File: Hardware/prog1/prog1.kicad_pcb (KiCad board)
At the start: 2 copper layers, 16 x 21 mm, 6 parts, among them J1 Conn_01x02, SW1 SW_Push

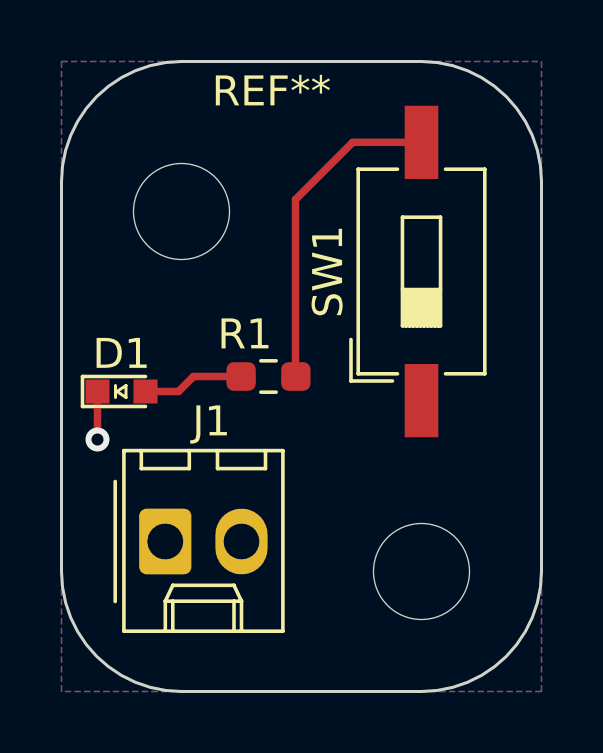
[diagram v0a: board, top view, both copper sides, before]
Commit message: rmved template proj files, added power flags, hidden ref. designators on silkscreen layer
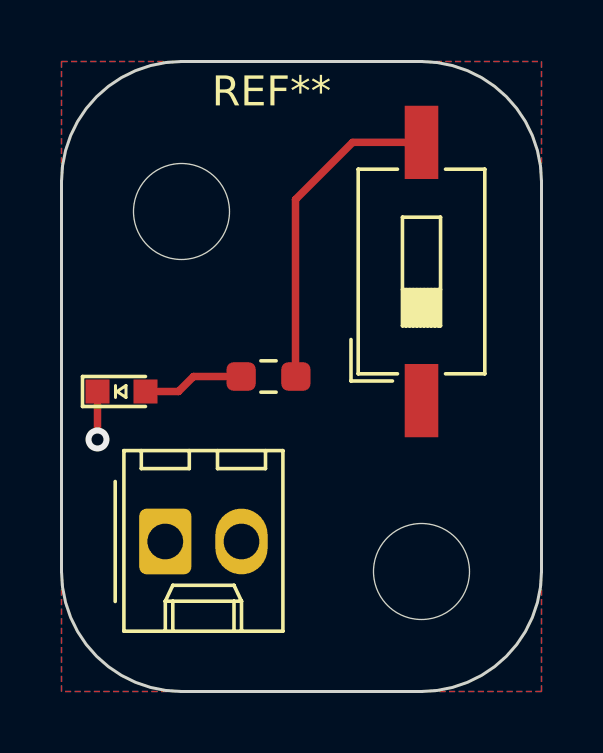
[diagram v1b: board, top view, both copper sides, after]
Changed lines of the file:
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@@
     (property "ki_keywords" "switch normally-open pushbutton push-button")
     (attr smd)
-    (fp_text reference "SW1" (at 0 -3.11 90) (layer "F.SilkS")
+    (fp_text reference "SW1" (at 0 -3.11 90) (layer "F.SilkS") hide
         (effects (font (size 1 1) (thickness 0.15)))
     )
@@
         (effects (font (size 1 1) (thickness 0.15)))
     )
-    (fp_text user "${REFERENCE}" (at 2.58 0) (layer "F.Fab")
+    (fp_text user "${REFERENCE}" (at 2.58 0) (layer "F.Fab") hide
         (effects (font (size 0.6 0.6) (thickness 0.09)))
     )
-    (fp_text user "on" (at 0.4275 -1.3425 90) (layer "F.Fab")
+    (fp_text user "on" (at 0.4275 -1.3425 90) (layer "F.Fab") hide
         (effects (font (size 0.6 0.6) (thickness 0.09)))
     )
@@
     (property "ki_keywords" "connector")
     (attr through_hole)
-    (fp_text reference "J1" (at 1.54 -4) (layer "F.SilkS")
+    (fp_text reference "J1" (at 1.54 -4) (layer "F.SilkS") hide
         (effects (font (size 1 1) (thickness 0.15)))
     )
@@
     (property "ki_keywords" "R res resistor")
     (attr smd)
-    (fp_text reference "R1" (at 0.7875 1.4) (layer "F.SilkS")
+    (fp_text reference "R1" (at 0.7875 1.4) (layer "F.SilkS") hide
         (effects (font (size 1 1) (thickness 0.15)))
     )
@@
         (effects (font (size 1 1) (thickness 0.15)))
     )
-    (fp_text user "${REFERENCE}" (at 0 0) (layer "F.Fab")
+    (fp_text user "${REFERENCE}" (at 0 0) (layer "F.Fab") hide
         (effects (font (size 0.4 0.4) (thickness 0.06)))
     )
@@
     (property "ki_keywords" "LED diode")
     (attr smd)
-    (fp_text reference "D1" (at 0 -1.25) (layer "F.SilkS")
-        (effects (font (size 1 1) (thickness 0.15)))
-    )
+    (fp_text reference "D1" (at 0 -1.25) (layer "F.SilkS") hide
+        (effects (font (size 1 1) (thickness 0.15)))
+    )

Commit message: changed footprint of LED to D_0603
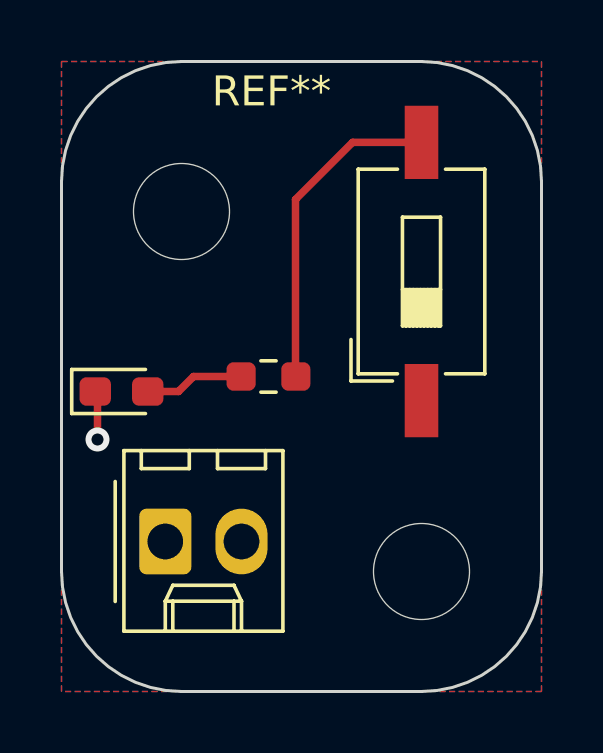
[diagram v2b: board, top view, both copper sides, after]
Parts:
- D1: footprint layout:LED_0603_Symbol_on_F.SilkS -> Diode_SMD:D_0603_1608Metric_Pad1.05x0.95mm_HandSolder
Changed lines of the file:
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@@
     (descr "Resistor SMD 0603 (1608 Metric), square (rectangular) end terminal, IPC_7351 nominal with elongated pad for handsoldering. (Body size source: IPC-SM-782 page 72, https://www.pcb-3d.com/wordpress/wp-content/uploads/ipc-sm-782a_amendment_1_and_2.pdf), generated with kicad-footprint-generator")
     (tags "resistor handsolder")
-    (property "MPN" "")
+    (property "MPN" "RES 105 OHM 1/10W 5% AXIAL")
     (property "Notes" "")
     (property "Sheetfile" "prog1.kicad_sch")
@@
     )
   )
-  (footprint "layout:LED_0603_Symbol_on_F.SilkS" (layer "F.Cu")
+  (footprint "Diode_SMD:D_0603_1608Metric_Pad1.05x0.95mm_HandSolder" (layer "F.Cu")
     (at 136 87)
-    (descr "LED 0603 smd package")
-    (tags "LED led 0603 SMD smd SMT smt smdled SMDLED smtled SMTLED")
-    (property "MPN" "")
+    (descr "Diode SMD 0603 (1608 Metric), square (rectangular) end terminal, IPC_7351 nominal, (Body size source: http://www.tortai-tech.com/upload/download/2011102023233369053.pdf), generated with kicad-footprint-generator")
+    (tags "diode handsolder")
+    (property "MPN" "LED RED CLEAR 0603 SMD")
     (property "Notes" "")
     (property "Sheetfile" "prog1.kicad_sch")
@@
     (property "ki_keywords" "LED diode")
     (attr smd)
-    (fp_text reference "D1" (at 0 -1.25) (layer "F.SilkS") hide
+    (fp_text reference "D1" (at 0 -1.43) (layer "F.SilkS") hide
         (effects (font (size 1 1) (thickness 0.15)))
     )
-    (fp_text value "LED_RED" (at 0 1.35) (layer "F.Fab") hide
+    (fp_text value "LED_RED" (at 0 1.43) (layer "F.Fab") hide
         (effects (font (size 1 1) (thickness 0.15)))
     )
-    (fp_line (start -1.3 -0.5) (end -1.3 0.5)
+    (fp_text user "${REFERENCE}" (at 0 0) (layer "F.Fab") hide
+        (effects (font (size 0.4 0.4) (thickness 0.06)))
+    )
+    (fp_line (start -1.66 -0.735) (end -1.66 0.735)
       (stroke (width 0.12) (type solid)) (layer "F.SilkS"))
-    (fp_line (start -1.3 -0.5) (end 0.8 -0.5)
+    (fp_line (start -1.66 0.735) (end 0.8 0.735)
       (stroke (width 0.12) (type solid)) (layer "F.SilkS"))
-    (fp_line (start -1.3 0.5) (end 0.8 0.5)
+    (fp_line (start 0.8 -0.735) (end -1.66 -0.735)
       (stroke (width 0.12) (type solid)) (layer "F.SilkS"))
-    (fp_line (start -0.2 -0.2) (end -0.2 0.2)
-      (stroke (width 0.1) (type solid)) (layer "F.SilkS"))
-    (fp_line (start -0.15 0) (end 0.15 -0.2)
-      (stroke (width 0.1) (type solid)) (layer "F.SilkS"))
-    (fp_line (start 0.15 -0.2) (end 0.15 0.2)
-      (stroke (width 0.1) (type solid)) (layer "F.SilkS"))
-    (fp_line (start 0.15 0.2) (end -0.15 0)
-      (stroke (width 0.1) (type solid)) (layer "F.SilkS"))
-    (fp_line (start -1.45 -0.65) (end 1.45 -0.65)
+    (fp_line (start -1.65 -0.73) (end 1.65 -0.73)
       (stroke (width 0.05) (type solid)) (layer "F.CrtYd"))
-    (fp_line (start -1.45 0.65) (end -1.45 -0.65)
+    (fp_line (start -1.65 0.73) (end -1.65 -0.73)
       (stroke (width 0.05) (type solid)) (layer "F.CrtYd"))
-    (fp_line (start 1.45 -0.65) (end 1.45 0.65)
+    (fp_line (start 1.65 -0.73) (end 1.65 0.73)
       (stroke (width 0.05) (type solid)) (layer "F.CrtYd"))
-    (fp_line (start 1.45 0.65) (end -1.45 0.65)
+    (fp_line (start 1.65 0.73) (end -1.65 0.73)
       (stroke (width 0.05) (type solid)) (layer "F.CrtYd"))
-    (fp_line (start -0.8 -0.4) (end 0.8 -0.4)
+    (fp_line (start -0.8 -0.1) (end -0.8 0.4)
       (stroke (width 0.1) (type solid)) (layer "F.Fab"))
-    (fp_line (start -0.8 0.4) (end -0.8 -0.4)
+    (fp_line (start -0.8 0.4) (end 0.8 0.4)
       (stroke (width 0.1) (type solid)) (layer "F.Fab"))
-    (fp_line (start 0.8 -0.4) (end 0.8 0.4)
+    (fp_line (start -0.5 -0.4) (end -0.8 -0.1)
       (stroke (width 0.1) (type solid)) (layer "F.Fab"))
-    (fp_line (start 0.8 0.4) (end -0.8 0.4)
+    (fp_line (start 0.8 -0.4) (end -0.5 -0.4)
       (stroke (width 0.1) (type solid)) (layer "F.Fab"))
-    (pad "1" smd rect (at -0.8 0 180) (size 0.8 0.8) (layers "F.Cu" "F.Paste" "F.Mask")
+    (fp_line (start 0.8 0.4) (end 0.8 -0.4)
+      (stroke (width 0.1) (type solid)) (layer "F.Fab"))
+    (pad "1" smd roundrect (at -0.875 0) (size 1.05 0.95) (layers "F.Cu" "F.Paste" "F.Mask") (roundrect_rratio 0.25)
       (net 1 "GND") (pinfunction "K") (pintype "passive"))
-    (pad "2" smd rect (at 0.8 0 180) (size 0.8 0.8) (layers "F.Cu" "F.Paste" "F.Mask")
+    (pad "2" smd roundrect (at 0.875 0) (size 1.05 0.95) (layers "F.Cu" "F.Paste" "F.Mask") (roundrect_rratio 0.25)
       (net 2 "Net-(D1-A)") (pinfunction "A") (pintype "passive"))
-    (model "${KISYS3DMOD}/LEDs.3dshapes/LED_0603.wrl"
+    (model "${KICAD6_3DMODEL_DIR}/Diode_SMD.3dshapes/D_0603_1608Metric.wrl"
       (offset (xyz 0 0 0))
       (scale (xyz 1 1 1))
-      (rotate (xyz 0 0 180))
+      (rotate (xyz 0 0 0))
     )
   )
